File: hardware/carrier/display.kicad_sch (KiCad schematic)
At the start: 2 parts, among them J3 PANEL

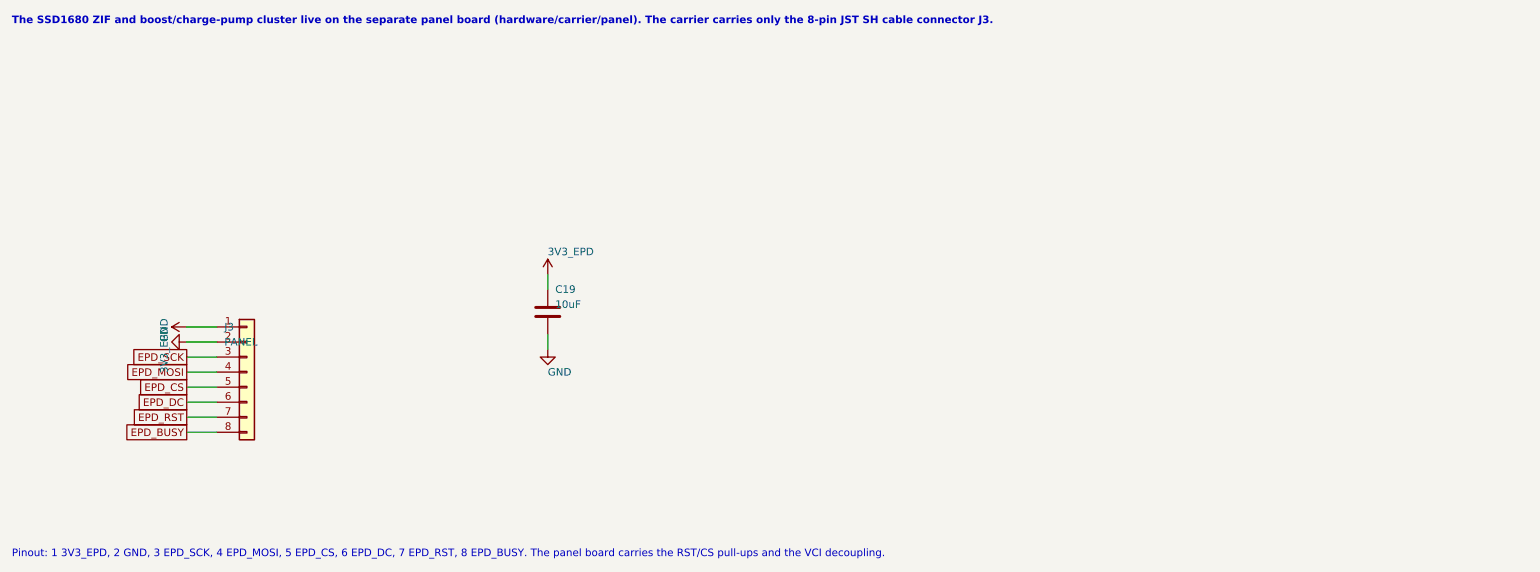
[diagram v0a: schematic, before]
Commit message: hardware/carrier: front light is the GDEY029T94-FL03 (6-pin flex -> FH34SRJ-6S on the panel board, anode/cathode over a 10-way SH cable, 33R 1206 + Q4 PWM drive replaces the NSI45020), front-light button SW2 on IO4 (FL_BTN), low-profile pass (FH34SRJ 1.0 mm ZIFs, 2 x 100uF 0805 instead of the 2.5 mm 1210, part-height table), sleep-current audit (Q1 gate pull-up 100k -> 2.2M: 38 -> 1.9 uA; SN74LVC2G126 moved to the bus-powered BRG_VDD rail: 0 on battery; table in the README), TPS62840 has no fixed-3.3 V variant (README). Custom FH34SRJ footprints from the Hirose catalog; LCSC numbers via the JLCPCB parts API. Both boards re-placed and re-routed: 0 unconnected, 0 clearance/courtyard errors, silk notes only; ERC 0/0; exports refreshed (owner, 17 Oct 2026)
Co-Authored-By: Claude Fable 5.1 <noreply@anthropic.com>
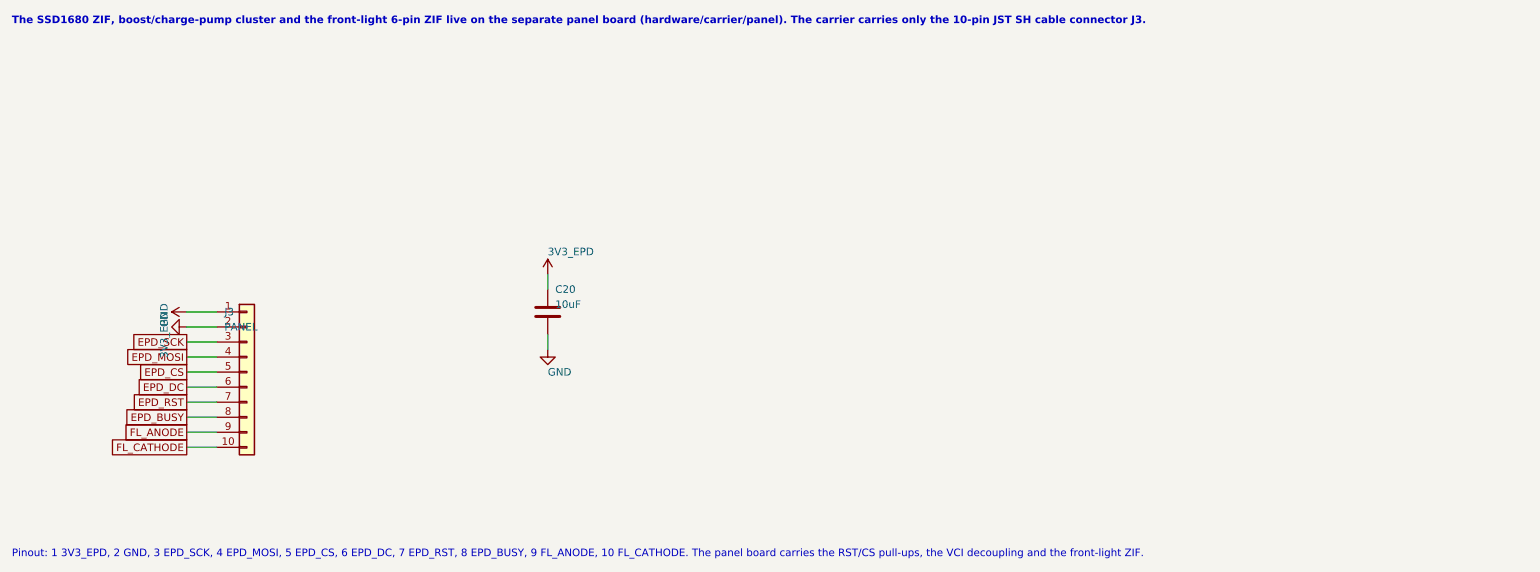
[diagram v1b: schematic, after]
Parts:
- removed C19: 10uF, Capacitor_SMD:C_0603_1608Metric, symbol Device:C
- added C20: 10uF, Capacitor_SMD:C_0603_1608Metric, symbol Device:C
- J3: footprint Connector_JST:JST_SH_SM08B-SRSS-TB_1x08-1MP_P1.00mm_Horizontal -> Connector_JST:JST_SH_SM10B-SRSS-TB_1x10-1MP_P1.00mm_Horizontal; symbol Connector_Generic:Conn_01x08 -> Connector_Generic:Conn_01x10; LCSC C160407 -> C160409; MPN SM08B-SRSS-TB -> SM10B-SRSS-TB; Note to panel board J2, 1:1 cable -> to panel board J2, 1:1 10-way SH cable
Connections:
- net 3V3_EPD: now also C20.1
- net GND: now also C20.2
- new net FL_ANODE: J3.9 (Pin_9)
- new net FL_CATHODE: J3.10 (Pin_10)
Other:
- note added: "Pinout: 1 3V3_EPD, 2 GND, 3 EPD_SCK, 4 EPD_MOSI, 5 EPD_CS, 6 EPD_DC, 7 EPD_RST, 8 EPD_BUSY, 9 FL_ANODE, 10 FL_CATHODE. The panel board carries the RST/CS pull-ups, the VCI decoupling and the front-light ZIF."
- note added: "The SSD1680 ZIF, boost/charge-pump cluster and the front-light 6-pin ZIF live on the separate panel board (hardware/carrier/panel). The carrier carries only the 10-pin JST SH cable connector J3."
- note removed: "Pinout: 1 3V3_EPD, 2 GND, 3 EPD_SCK, 4 EPD_MOSI, 5 EPD_CS, 6 EPD_DC, 7 EPD_RST, 8 EPD_BUSY. The panel board carries the RST/CS pull-ups and the VCI decoupling."
- note removed: "The SSD1680 ZIF and boost/charge-pump cluster live on the separate panel board (hardware/carrier/panel). The carrier carries only the 8-pin JST SH cable connector J3."
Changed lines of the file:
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@@
 		(company "awong-dev/pager")
 	)
-	(text "The SSD1680 ZIF and boost/charge-pump cluster live on the separate panel board (hardware/carrier/panel). The carrier carries only the 8-pin JST SH cable connector J3."
+	(text "The SSD1680 ZIF, boost/charge-pump cluster and the front-light 6-pin ZIF live on the separate panel board (hardware/carrier/panel). The carrier carries only the 10-pin JST SH cable connector J3."
 		(exclude_from_sim no)
 		(at 20 20 0)
@@
 	(wire
 		(pts
+			(xy 54.61 69.85)
+			(xy 49.53 69.85)
+		)
+		(stroke
+			(width 0)
+			(type default)
+		)
+	)
+	(wire
+		(pts
 			(xy 54.61 72.39)
 			(xy 49.53 72.39)
@@
 		)
 	)
+	(global_label "EPD_SCK"
+		(shape passive)
+		(at 49.53 74.93 180)
+		(fields_autoplaced yes)
+		(effects
+			(font
+				(size 1.27 1.27)
+			)
+			(justify right)
+		)
+	)
 	(wire
 		(pts
@@
 		)
 	)
-	(global_label "EPD_SCK"
+	(global_label "EPD_MOSI"
 		(shape passive)
 		(at 49.53 77.47 180)
@@
 		)
 	)
-	(global_label "EPD_MOSI"
+	(global_label "EPD_CS"
 		(shape passive)
 		(at 49.53 80.01 180)
@@
 		)
 	)
-	(global_label "EPD_CS"
+	(global_label "EPD_DC"
 		(shape passive)
 		(at 49.53 82.55 180)
@@
 		)
 	)
-	(global_label "EPD_DC"
+	(global_label "EPD_RST"
 		(shape passive)
 		(at 49.53 85.09 180)
@@
 		)
 	)
-	(global_label "EPD_RST"
+	(global_label "EPD_BUSY"
 		(shape passive)
 		(at 49.53 87.63 180)
@@
 		)
 	)
-	(global_label "EPD_BUSY"
+	(global_label "FL_ANODE"
 		(shape passive)
 		(at 49.53 90.17 180)
+		(fields_autoplaced yes)
+		(effects
+			(font
+				(size 1.27 1.27)
+			)
+			(justify right)
+		)
+	)
+	(wire
+		(pts
+			(xy 54.61 92.71)
+			(xy 49.53 92.71)
+		)
+		(stroke
+			(width 0)
+			(type default)
+		)
+	)
+	(global_label "FL_CATHODE"
+		(shape passive)
+		(at 49.53 92.71 180)
 		(fields_autoplaced yes)
 		(effects
@@
 		)
 	)
-	(text "Pinout: 1 3V3_EPD, 2 GND, 3 EPD_SCK, 4 EPD_MOSI, 5 EPD_CS, 6 EPD_DC, 7 EPD_RST, 8 EPD_BUSY. The panel board carries the RST/CS pull-ups and the VCI decoupling."
+	(text "Pinout: 1 3V3_EPD, 2 GND, 3 EPD_SCK, 4 EPD_MOSI, 5 EPD_CS, 6 EPD_DC, 7 EPD_RST, 8 EPD_BUSY, 9 FL_ANODE, 10 FL_CATHODE. The panel board carries the RST/CS pull-ups, the VCI decoupling and the front-light ZIF."
 		(exclude_from_sim no)
 		(at 20 110 0)
@@
 	)
 	(symbol
-		(lib_id "Connector_Generic:Conn_01x08")
+		(lib_id "Connector_Generic:Conn_01x10")
 		(at 59.69 80.01 0)
 		(unit 1)
@@
 		(dnp no)
 		(property "Reference" "J3"
+			(at 55.88 69.85 0)
+			(effects
+				(font
+					(size 1.27 1.27)
+				)
+				(justify left)
+			)
+		)
+		(property "Value" "PANEL"
 			(at 55.88 72.39 0)
 			(effects
@@
 			)
 		)
-		(property "Value" "PANEL"
+		(property "Footprint" "Connector_JST:JST_SH_SM10B-SRSS-TB_1x10-1MP_P1.00mm_Horizontal"
 			(at 55.88 74.93 0)
-			(effects
-				(font
-					(size 1.27 1.27)
-				)
-				(justify left)
-			)
-		)
-		(property "Footprint" "Connector_JST:JST_SH_SM08B-SRSS-TB_1x08-1MP_P1.00mm_Horizontal"
+			(hide yes)
+			(effects
+				(font
+					(size 1.27 1.27)
+				)
+				(justify left)
+			)
+		)
+		(property "Datasheet" "~"
 			(at 55.88 77.47 0)
 			(hide yes)
@@
 			)
 		)
-		(property "Datasheet" "~"
+		(property "Description" "Generic connector, single row, 01x10, script generated (kicad-library-utils/schlib/autogen/connector/)"
 			(at 55.88 80.01 0)
 			(hide yes)
@@
 			)
 		)
-		(property "Description" "Generic connector, single row, 01x08, script generated (kicad-library-utils/schlib/autogen/connector/)"
-			(at 55.88 82.55 0)
-			(hide yes)
-			(effects
-				(font
-					(size 1.27 1.27)
-				)
-				(justify left)
-			)
-		)
-		(property "MPN" "SM08B-SRSS-TB"
+		(property "MPN" "SM10B-SRSS-TB"
 			(at 59.69 95.25 0)
 			(hide yes)
@@
 			)
 		)
-		(property "LCSC" "C160407"
+		(property "LCSC" "C160409"
 			(at 59.69 97.79 0)
 			(hide yes)
@@
 			)
 		)
-		(property "Note" "to panel board J2, 1:1 cable"
+		(property "Note" "to panel board J2, 1:1 10-way SH cable"
 			(at 59.69 102.87 0)
 			(hide yes)
@@
 		)
 		(pin "8"
+		)
+		(pin "9"
+		)
+		(pin "10"
 		)
 		(instances
@@
 	(symbol
 		(lib_id "pager-carrier:PWR_3V3_EPD")
-		(at 49.53 72.39 90)
+		(at 49.53 69.85 90)
 		(unit 1)
 		(exclude_from_sim no)
@@
 		(dnp no)
 		(property "Reference" "#PWR109"
-			(at 49.53 72.39 0)
+			(at 49.53 69.85 0)
 			(hide yes)
 			(effects
@@
 		)
 		(property "Value" "3V3_EPD"
-			(at 45.72 72.39 0)
+			(at 45.72 69.85 0)
 			(effects
 				(font
@@
 		)
 		(property "Footprint" ""
-			(at 49.53 72.39 0)
+			(at 49.53 69.85 0)
 			(hide yes)
 			(effects
@@
 		)
 		(property "Datasheet" "~"
-			(at 49.53 72.39 0)
+			(at 49.53 69.85 0)
 			(hide yes)
 			(effects
@@
 		)
 		(property "Description" "Power symbol"
-			(at 49.53 72.39 0)
+			(at 49.53 69.85 0)
 			(hide yes)
 			(effects
@@
 	(symbol
 		(lib_id "power:GND")
-		(at 49.53 74.93 270)
+		(at 49.53 72.39 270)
 		(unit 1)
 		(exclude_from_sim no)
@@
 		(dnp no)
 		(property "Reference" "#PWR110"
-			(at 49.53 74.93 0)
+			(at 49.53 72.39 0)
 			(hide yes)
 			(effects
@@
 		)
 		(property "Value" "GND"
-			(at 45.72 74.93 0)
+			(at 45.72 72.39 0)
 			(effects
 				(font
@@
 		)
 		(property "Footprint" ""
-			(at 49.53 74.93 0)
+			(at 49.53 72.39 0)
 			(hide yes)
 			(effects
@@
 		)
 		(property "Datasheet" "~"
-			(at 49.53 74.93 0)
+			(at 49.53 72.39 0)
 			(hide yes)
 			(effects
@@
 		)
 		(property "Description" "Power symbol"
-			(at 49.53 74.93 0)
+			(at 49.53 72.39 0)
 			(hide yes)
 			(effects
@@
 		(in_pos_files yes)
 		(dnp no)
-		(property "Reference" "C19"
+		(property "Reference" "C20"
 			(at 111.76 66.04 0)
 			(effects
@@
 			(project "pager-carrier"
 				(path "/10ec5e8c-30f8-50c5-8dd4-a077611d8ec6/4f9993a7-c2ec-5512-8944-2a1ee7e389ea"
-					(reference "C19")
+					(reference "C20")
 					(unit 1)
 				)
